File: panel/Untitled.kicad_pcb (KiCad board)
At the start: 2 copper layers, 30.2 x 128.5 mm, 1 part

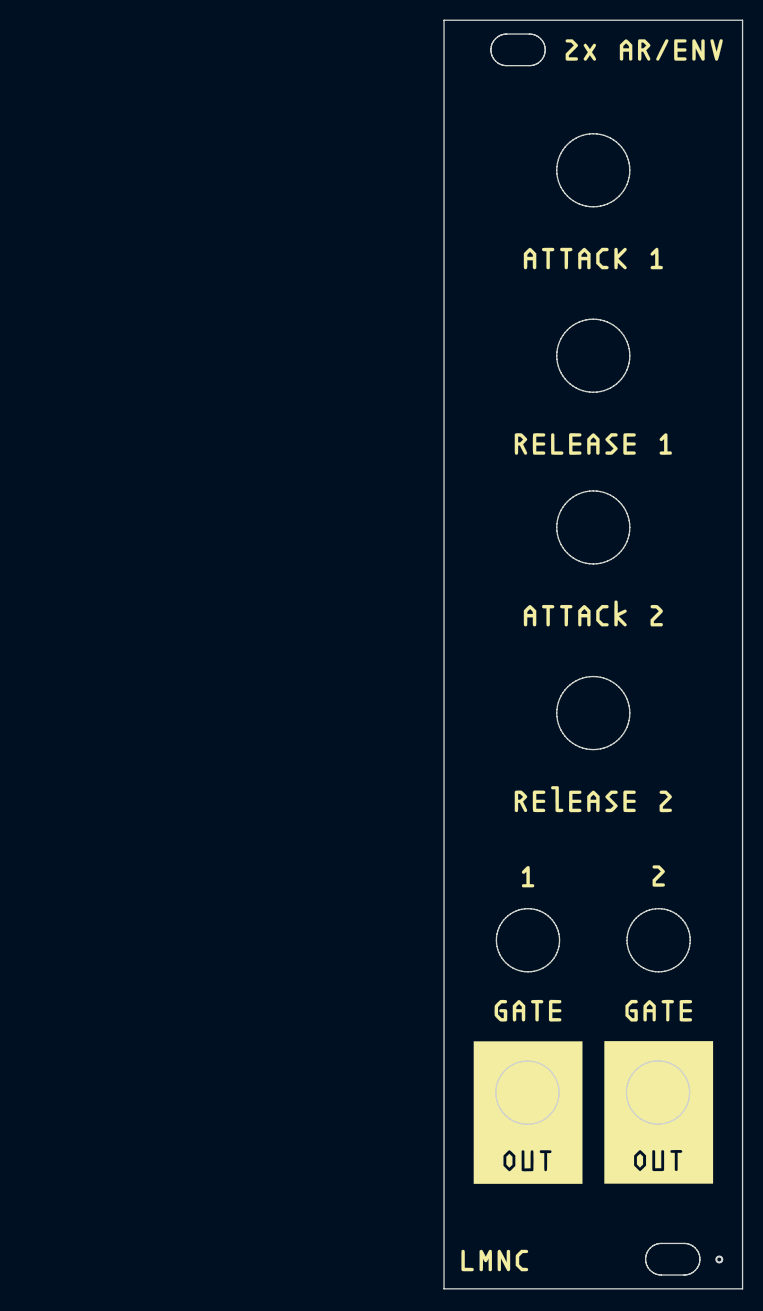
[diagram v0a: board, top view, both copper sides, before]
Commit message: Use right panel
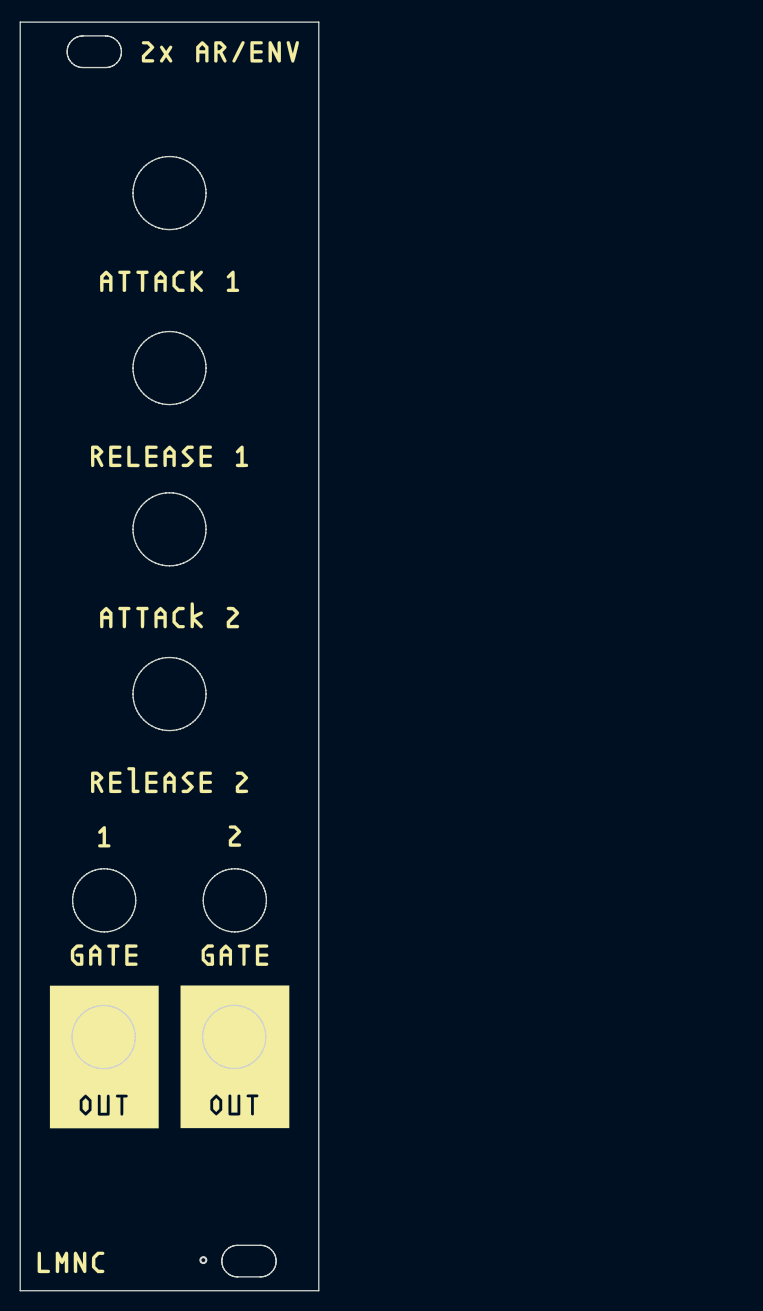
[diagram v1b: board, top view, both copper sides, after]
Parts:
- moved Ref** 42.9 mm to (106.0, 104.6)
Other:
- outline, holes or cut-outs redrawn
